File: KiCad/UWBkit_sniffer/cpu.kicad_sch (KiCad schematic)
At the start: 24 parts, among them J6 Conn_SWD, J7 Conn_GPIO, SW1 SW_Push, T1 TestPoint_Small, T2 TestPoint_Small, T3 TestPoint_Small, T4 TestPoint_Small, T5 TestPoint_Small, U1 LBUA5QJ2AB

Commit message: Redone RF trace, repositioned UWC.20 and mounting holes
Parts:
- C5: footprint Capacitor_SMD:C_0402_1005Metric -> Capacitor_SMD:C_0603_1608Metric
- L1, L2: footprint Inductor_SMD:L_0402_1005Metric -> Inductor_SMD:L_0603_1608Metric
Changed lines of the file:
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@@
 			)
 		)
-		(property "Footprint" "Inductor_SMD:L_0402_1005Metric"
+		(property "Footprint" "Inductor_SMD:L_0603_1608Metric"
 			(at 261.62 68.58 0)
 			(effects
@@
 			)
 		)
-		(property "Footprint" "Capacitor_SMD:C_0402_1005Metric"
+		(property "Footprint" "Capacitor_SMD:C_0603_1608Metric"
 			(at 257.81 63.5 0)
 			(effects
@@
 			)
 		)
-		(property "Footprint" "Inductor_SMD:L_0402_1005Metric"
+		(property "Footprint" "Inductor_SMD:L_0603_1608Metric"
 			(at 254 68.58 0)
 			(effects

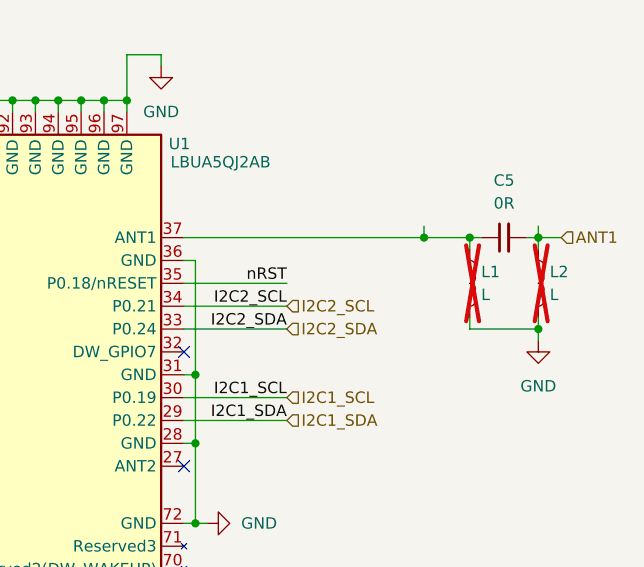
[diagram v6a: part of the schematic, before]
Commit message: Moved pi-filter past R8 shorting resistor
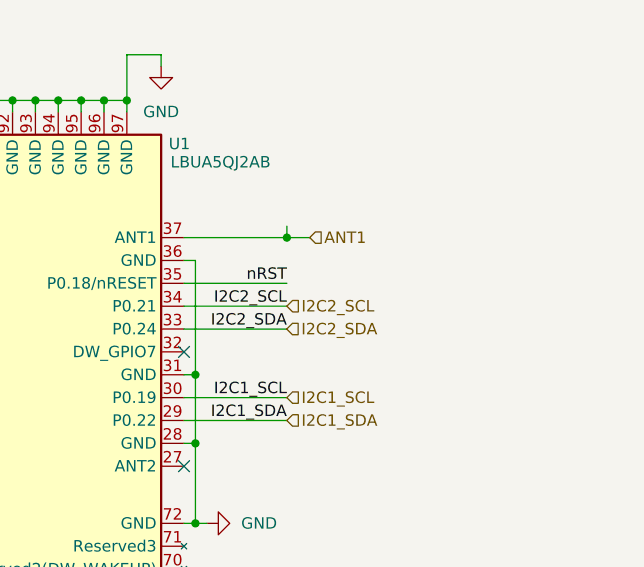
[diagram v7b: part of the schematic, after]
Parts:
- removed C5: 0R, Capacitor_SMD:C_0603_1608Metric, symbol Device:C_Small
- removed L1, L2: L, Inductor_SMD:L_0603_1608Metric, symbol Device:L
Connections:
- net ANT1: now also U1.37 (ANT1)

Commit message: Release V1.0
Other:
- title: (none) -> CPU
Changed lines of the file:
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@@
 	(generator_version "9.0")
 	(paper "A4")
+	(title_block
+		(title "CPU")
+		(date "2026-02-24")
+		(rev "1.0")
+	)
 	(text "Power"
 		(exclude_from_sim no)
